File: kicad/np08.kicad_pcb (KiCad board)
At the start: 2 copper layers, 101.6 x 101.6 mm, 60 parts, among them P1 USB_B, P10 CONN_01X02, P11 CONN_01X02, P12 analog, P13 GND, P14 +5V, P15 CONN_01X08, P16 CONN_01X08, P2 CONN_01X04, P3 aliment., P4 sw_aliment, P5 sw_pic, P6 CONN_01X03, P7 CONN_01X03, P8 CONN_01X02, P9 CONN_01X02, SW1 SW_PUSH, U1 LM78L05ACZ, U2 LM7805CT, U3 L293D, U4 ULN2803, Y1 Crystal

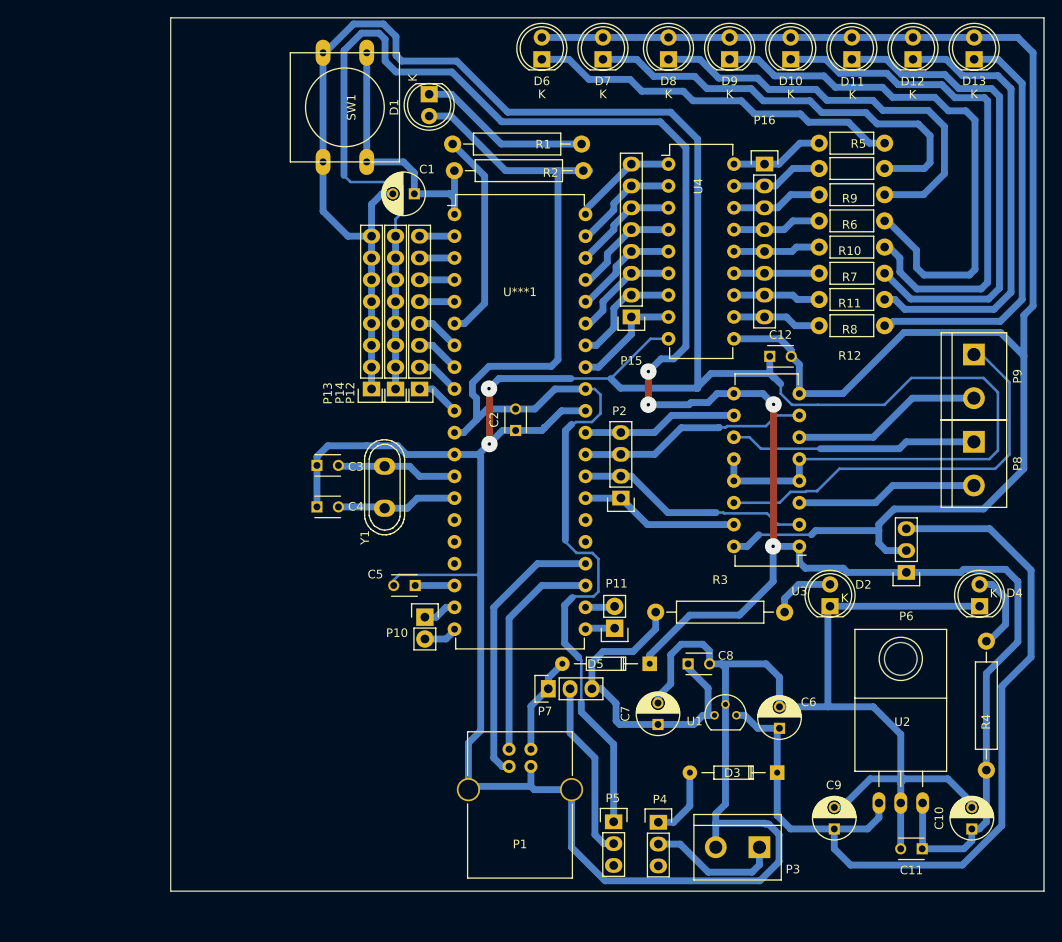
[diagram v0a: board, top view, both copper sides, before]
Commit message: cambios en la placa np08
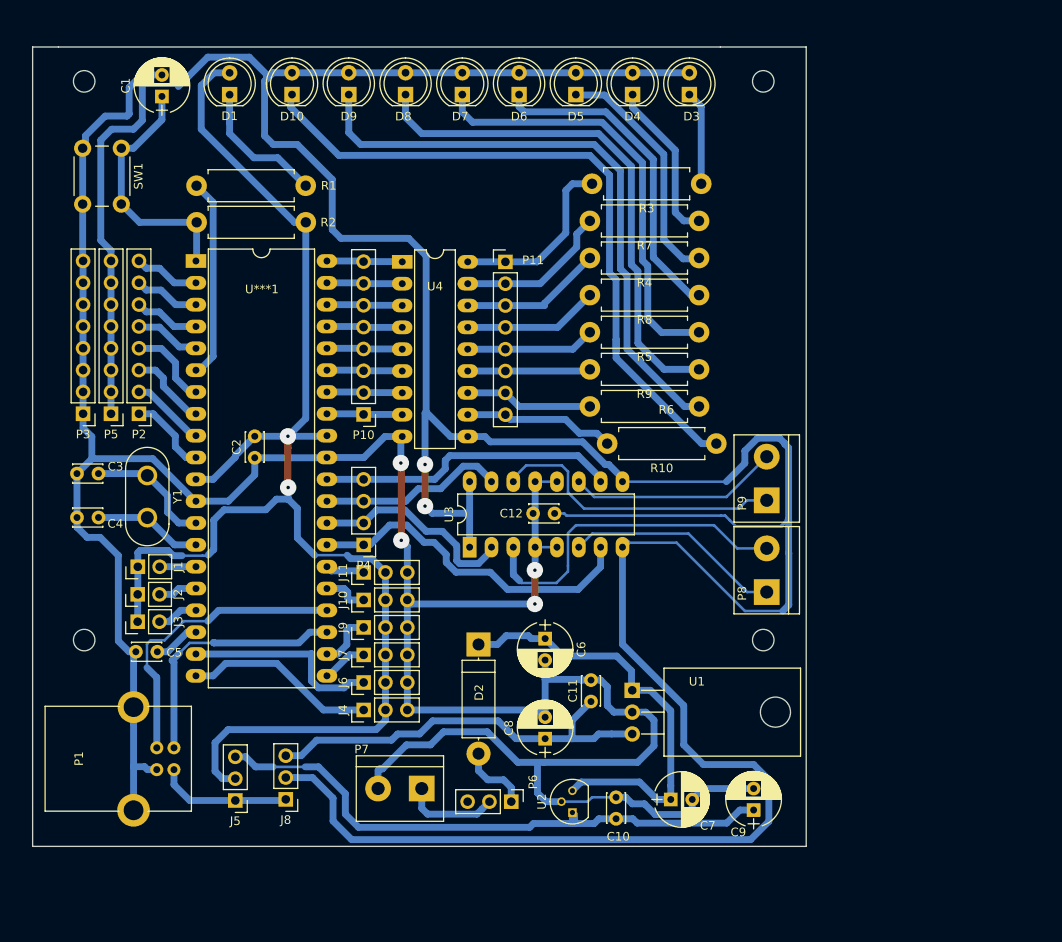
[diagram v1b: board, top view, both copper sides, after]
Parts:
- removed D11, D12, D13: LED, LEDs:LED-5MM
- removed P12: analog, Pin_Headers:Pin_Header_Straight_1x08
- removed P13: GND, Pin_Headers:Pin_Header_Straight_1x08
- removed P14: +5V, Pin_Headers:Pin_Header_Straight_1x08
- removed P15, P16: CONN_01X08, Pin_Headers:Pin_Header_Straight_1x08
- removed R11, R12: R, Resistors_ThroughHole:Resistor_Horizontal_RM7mm
- added ?: 2.5mm, Mounting_Holes:MountingHole_2.5mm, F.Cu at (89.0, 127.0)
- added ?: 2.5mm, Mounting_Holes:MountingHole_2.5mm, F.Cu at (168.0, 127.0)
- added ?: 2.5mm, Mounting_Holes:MountingHole_2.5mm, F.Cu at (168.0, 62.0)
- added ?: 2.5mm, Mounting_Holes:MountingHole_2.5mm, F.Cu at (89.0, 62.0)
- added J1: SENS_D3, Pin_Headers:Pin_Header_Straight_1x02_Pitch2.54mm, F.Cu at (95.2, 118.5)
- added J10: SRV2, Pin_Headers:Pin_Header_Straight_1x03_Pitch2.54mm, F.Cu at (121.5, 122.3)
- added J11: SRV1, Pin_Headers:Pin_Header_Straight_1x03_Pitch2.54mm, F.Cu at (121.5, 119.1)
- added J2: SENS_D2, Pin_Headers:Pin_Header_Straight_1x02_Pitch2.54mm, F.Cu at (95.2, 121.7)
- added J3: SENS_D1, Pin_Headers:Pin_Header_Straight_1x02_Pitch2.54mm, F.Cu at (95.2, 124.9)
- added J4: SRV6, Pin_Headers:Pin_Header_Straight_1x03_Pitch2.54mm, F.Cu at (121.5, 135.1)
- added J5: USB-78L05, Pin_Headers:Pin_Header_Straight_1x03_Pitch2.54mm, F.Cu at (106.6, 145.7)
- added J6: SRV5, Pin_Headers:Pin_Header_Straight_1x03_Pitch2.54mm, F.Cu at (121.5, 131.9)
- added J7: SRV4, Pin_Headers:Pin_Header_Straight_1x03_Pitch2.54mm, F.Cu at (121.5, 128.7)
- added J8: USB-LM7805, Pin_Headers:Pin_Header_Straight_1x03_Pitch2.54mm, F.Cu at (112.5, 145.5)
- added J9: SRV3, Pin_Headers:Pin_Header_Straight_1x03_Pitch2.54mm, F.Cu at (121.5, 125.5)
- C1, C6: footprint Capacitors_ThroughHole:C_Radial_D5_L6_P2.5 -> Capacitors_THT:CP_Radial_D6.3mm_P2.50mm
- C10: value 100 uF-electr -> 0.1uF; footprint Capacitors_ThroughHole:C_Radial_D5_L6_P2.5 -> Capacitors_THT:C_Disc_D3.4mm_W2.1mm_P2.50mm
- C11, C12, C2, C3, C4, C5: footprint Capacitors_ThroughHole:C_Disc_D3_P2.5 -> Capacitors_THT:C_Disc_D3.4mm_W2.1mm_P2.50mm
- C7: value 100 uF-electr -> 100uF-electr; footprint Capacitors_ThroughHole:C_Radial_D5_L6_P2.5 -> Capacitors_THT:CP_Radial_D6.3mm_P2.50mm
- C8: value 0.1uF -> 100 uF-electr; footprint Capacitors_ThroughHole:C_Disc_D3_P2.5 -> Capacitors_THT:CP_Radial_D6.3mm_P2.50mm
- C9: value 100uF-electr -> 100 uF-electr; footprint Capacitors_ThroughHole:C_Radial_D5_L6_P2.5 -> Capacitors_THT:CP_Radial_D6.3mm_P2.50mm
- D1: value LED -> RUN; footprint LEDs:LED-5MM -> LEDs:LED_D5.0mm
- D10: value LED -> LED_128; footprint LEDs:LED-5MM -> LEDs:LED_D5.0mm
- D2: value LED -> D; footprint LEDs:LED-5MM -> Diodes_THT:D_5W_P12.70mm_Horizontal
- D3: value D -> LED_1; footprint Diodes_ThroughHole:Diode_DO-35_SOD27_Horizontal_RM10 -> LEDs:LED_D5.0mm
- D4: value LED -> LED_2; footprint LEDs:LED-5MM -> LEDs:LED_D5.0mm
- D5: value D -> LED_4; footprint Diodes_ThroughHole:Diode_DO-35_SOD27_Horizontal_RM10 -> LEDs:LED_D5.0mm
- D6: value LED -> LED_8; footprint LEDs:LED-5MM -> LEDs:LED_D5.0mm
- D7: value LED -> LED_16; footprint LEDs:LED-5MM -> LEDs:LED_D5.0mm
- D8: value LED -> LED_32; footprint LEDs:LED-5MM -> LEDs:LED_D5.0mm
- D9: value LED -> LED_64; footprint LEDs:LED-5MM -> LEDs:LED_D5.0mm
- P1: footprint Connect:USB_B -> Connectors:USB_B
- P10, P11: value CONN_01X02 -> PORTB; footprint Pin_Headers:Pin_Header_Straight_1x02 -> Pin_Headers:Pin_Header_Straight_1x08_Pitch2.54mm
- P2: value CONN_01X04 -> analog; footprint Pin_Headers:Pin_Header_Straight_1x04 -> Pin_Headers:Pin_Header_Straight_1x08_Pitch2.54mm
- P3: value aliment. -> GND; footprint Connect:bornier2 -> Pin_Headers:Pin_Header_Straight_1x08_Pitch2.54mm
- P4: value sw_aliment -> PORTD=4-7; footprint Pin_Headers:Pin_Header_Straight_1x03 -> Pin_Headers:Pin_Header_Straight_1x04_Pitch2.54mm
- P5: value sw_pic -> +5V; footprint Pin_Headers:Pin_Header_Straight_1x03 -> Pin_Headers:Pin_Header_Straight_1x08_Pitch2.54mm
- P6: value CONN_01X03 -> sw_aliment; footprint Pin_Headers:Pin_Header_Straight_1x03 -> Pin_Headers:Pin_Header_Straight_1x03_Pitch2.54mm
- P7: value CONN_01X03 -> - +; footprint Pin_Headers:Pin_Header_Straight_1x03 -> Connectors:bornier2
- P8: value CONN_01X02 -> MOTOR_2; footprint Connect:bornier2 -> Connectors:bornier2
- P9: value CONN_01X02 -> MOTOR_1; footprint Connect:bornier2 -> Connectors:bornier2
- R1, R2: footprint Resistors_ThroughHole:Resistor_Horizontal_RM15mm -> Resistors_THT:R_Axial_DIN0411_L9.9mm_D3.6mm_P12.70mm_Horizontal
- R10, R5, R6, R7, R8, R9: footprint Resistors_ThroughHole:Resistor_Horizontal_RM7mm -> Resistors_THT:R_Axial_DIN0411_L9.9mm_D3.6mm_P12.70mm_Horizontal
- R3, R4: value 470 -> R; footprint Resistors_ThroughHole:Resistor_Horizontal_RM15mm -> Resistors_THT:R_Axial_DIN0411_L9.9mm_D3.6mm_P12.70mm_Horizontal
- SW1: value SW_PUSH -> RESET; footprint Buttons_Switches_ThroughHole:SW_PUSH-12mm -> Buttons_Switches_THT:SW_PUSH_6mm_h5mm
- U***1: footprint Housings_DIP:DIP-40_W15.24mm -> Housings_DIP:DIP-40_W15.24mm_LongPads
- U1: value LM78L05ACZ -> LM7805CT; footprint TO_SOT_Packages_THT:TO-92_Molded_Narrow -> TO_SOT_Packages_THT:TO-220_Horizontal
- U2: value LM7805CT -> LM78L05ACZ; footprint TO_SOT_Packages_THT:TO-220_Neutral123_Horizontal -> TO_SOT_Packages_THT:TO-92_Molded_Narrow
- U3: footprint Housings_DIP:DIP-16_W7.62mm -> Housings_DIP:DIP-16_W7.62mm_LongPads
- U4: footprint Housings_DIP:DIP-18_W7.62mm -> Housings_DIP:DIP-18_W7.62mm_LongPads
- Y1: footprint Crystals:Crystal_HC50-U_Vertical -> Crystals:Crystal_HC50_Vertical
- moved P3 91.3 mm to (88.9, 100.7)
- moved D3 79.5 mm to (159.4, 63.5), turned to 90 degrees
- moved P5 75.3 mm to (92.1, 100.7), turned to 180 degrees
- moved D4 71.9 mm to (152.8, 63.5)
- moved R4 68.3 mm to (160.5, 82.5), turned to 180 degrees
- moved D5 66.8 mm to (146.2, 63.5), turned to 90 degrees
- moved D10 58.2 mm to (113.2, 63.5)
- moved P2 56.9 mm to (95.4, 100.7)
- moved P6 53.1 mm to (138.7, 145.8), turned to 270 degrees
- moved R3 50.1 mm to (160.8, 73.9), turned to 180 degrees
- moved P4 47.1 mm to (121.5, 115.9), turned to 180 degrees
- moved D9 44.5 mm to (119.8, 63.5)
- moved P11 44.5 mm to (138.0, 83.0), turned to 0 degrees
- moved C11 42.2 mm to (148.0, 134.2), turned to 90 degrees
- moved P1 41.6 mm to (99.4, 142.1), turned to 180 degrees
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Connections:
- C10 pad 1: /alimentacion/5v_lm7805 -> 5v_reg_pic
- C11 pad 1: /alimentacion/5v_lm7805 -> 5v_reg
- C12 pad 2: /UNL2803/+5/12V -> 5v
- C7 pad 1: /alimentacion/5v_78l05 -> 12V
- C8 pad 1: /alimentacion/5v_78l05 -> 5v_reg
- C9 pad 1: 12V -> 5v_reg_pic
- D10 pad 2: /UNL2803/+5/12V -> 5v
- D2 pad 1: GND -> 12V
- D3 pad 1: 12V -> Net-(D3-Pad1)
- D3 pad 2: Net-(D3-Pad2) -> 5v
- D4 pad 1: GND -> Net-(D4-Pad1)
- D4 pad 2: Net-(D4-Pad2) -> 5v
- D5 pad 1: /alimentacion/5v_lm7805 -> Net-(D5-Pad1)
- D5 pad 2: VCC -> 5v
- D6 pad 2: /UNL2803/+5/12V -> 5v
- D7 pad 2: /UNL2803/+5/12V -> 5v
- D8 pad 2: /UNL2803/+5/12V -> 5v
- D9 pad 2: /UNL2803/+5/12V -> 5v
- P1 pad 1: VCC -> 5v_reg_usb
- P10 pad 1: RD0 -> IN7
- P10 pad 2: RD1 -> IN6
- P11 pad 1: RD2 -> OOUT_0
- P11 pad 2: RD3 -> OOUT_1
- P2 pad 1: RD4 -> Net-(P2-Pad1)
- P2 pad 2: RD5 -> Net-(P2-Pad2)
- P2 pad 3: RD6 -> Net-(P2-Pad3)
- P2 pad 4: RD7 -> Net-(P2-Pad4)
- P3 pad 1: Net-(P3-Pad1) -> GND
- P4 pad 1: Net-(D3-Pad2) -> RD4
- P4 pad 2: Net-(P3-Pad1) -> RD5
- P4 pad 3: (no net) -> RD6
- P5 pad 1: VDD -> 5v
- P5 pad 2: vcc_con -> 5v
- P5 pad 3: (no net) -> 5v
- P6 pad 1: /alimentacion/5v_lm7805 -> Net-(D2-Pad2)
- P6 pad 2: /UNL2803/+5/12V -> Net-(P6-Pad2)
- P6 pad 3: 12V -> (no net)
- P7 pad 1: VCC -> Net-(P6-Pad2)
- P7 pad 2: vcc_con -> GND
- R10 pad 1: Net-(D9-Pad1) -> Net-(D10-Pad1)
- R10 pad 2: OOUT_3 -> OOUT_7
- R3 pad 1: /alimentacion/5v_78l05 -> Net-(D3-Pad1)
- R3 pad 2: Net-(D2-Pad2) -> OOUT_0
- R4 pad 1: /alimentacion/5v_lm7805 -> Net-(D5-Pad1)
- R4 pad 2: Net-(D4-Pad2) -> OOUT_2
- R5 pad 1: Net-(D6-Pad1) -> Net-(D7-Pad1)
- R5 pad 2: OOUT_0 -> OOUT_4
- R6 pad 1: Net-(D8-Pad1) -> Net-(D9-Pad1)
- R6 pad 2: OOUT_2 -> OOUT_6
- R7 pad 1: Net-(D10-Pad1) -> Net-(D4-Pad1)
- R7 pad 2: OOUT_4 -> OOUT_1
- R8 pad 1: Net-(D12-Pad1) -> Net-(D6-Pad1)
- R8 pad 2: OOUT_6 -> OOUT_3
- R9 pad 1: Net-(D7-Pad1) -> Net-(D8-Pad1)
- R9 pad 2: OOUT_1 -> OOUT_5
- U***1 pad 10: Net-(P12-Pad1) -> Net-(P2-Pad1)
- U***1 pad 15: (no net) -> RC0
- U***1 pad 16: (no net) -> RC1
- U***1 pad 17: (no net) -> RC2
- U***1 pad 2: Net-(P12-Pad8) -> Net-(P2-Pad8)
- U***1 pad 25: (no net) -> RC6
- U***1 pad 26: (no net) -> RC7
- U***1 pad 3: Net-(P12-Pad7) -> Net-(P2-Pad7)
- U***1 pad 4: Net-(P12-Pad6) -> Net-(P2-Pad6)
- U***1 pad 5: Net-(P12-Pad5) -> Net-(P2-Pad5)
- U***1 pad 7: Net-(P12-Pad4) -> Net-(P2-Pad4)
- U***1 pad 8: Net-(P12-Pad3) -> Net-(P2-Pad3)
- U***1 pad 9: Net-(P12-Pad2) -> Net-(P2-Pad2)
- U1 pad 1: /alimentacion/5v_78l05 -> 12V
- U1 pad 3: 12V -> 5v_reg
- U2 pad 1: 12V -> 5v_reg_pic
- U2 pad 3: /alimentacion/5v_lm7805 -> 12V
- U3 pad 1: /alimentacion/5v_lm7805 -> 5v
- U3 pad 11: Net-(P8-Pad1) -> Net-(P9-Pad2)
- U3 pad 15: RD4 -> RD6
- U3 pad 16: /UNL2803/+5/12V -> 5v
- U3 pad 6: Net-(P9-Pad2) -> Net-(P8-Pad1)
- U3 pad 7: RD6 -> RD4
- U3 pad 8: /UNL2803/+5/12V -> 5v
- U3 pad 9: /alimentacion/5v_lm7805 -> 5v
- U4 pad 10: /UNL2803/+5/12V -> 5v
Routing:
- net 5v: track 0.00 -> 422.9 mm, vias 0 -> 2
- net /alimentacion/5v_lm7805: track 257.1 -> 0.00 mm, vias 4 -> 0
- net GND: track 543.2 -> 323.0 mm, vias 2 -> 4
- net /UNL2803/+5/12V: track 192.5 -> 0.00 mm
- net 5v_reg_pic: track 0.00 -> 68.7 mm
- net Net-(D11-Pad1): track 56.4 -> 0.00 mm
- net Net-(D12-Pad1): track 52.5 -> 0.00 mm
- net 12V: track 102.8 -> 50.6 mm
- net Net-(D13-Pad1): track 49.9 -> 0.00 mm
- net 5v_reg: track 0.00 -> 48.7 mm
- net /alimentacion/5v_78l05: track 38.6 -> 0.00 mm
- net VDD: track 138.9 -> 173.9 mm, vias 0 -> 2
- net Net-(D5-Pad1): track 0.00 -> 28.2 mm
- net RD4: track 18.5 -> 39.8 mm
- net vcc_con: track 20.8 -> 0.00 mm
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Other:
- board size 101.6 x 101.6 mm -> 90 x 93 mm
- net class fina: trace_width 0.3 -> 0.5

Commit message: arreglando la fuente de alimentación, los servos estaban conectados al 78l05
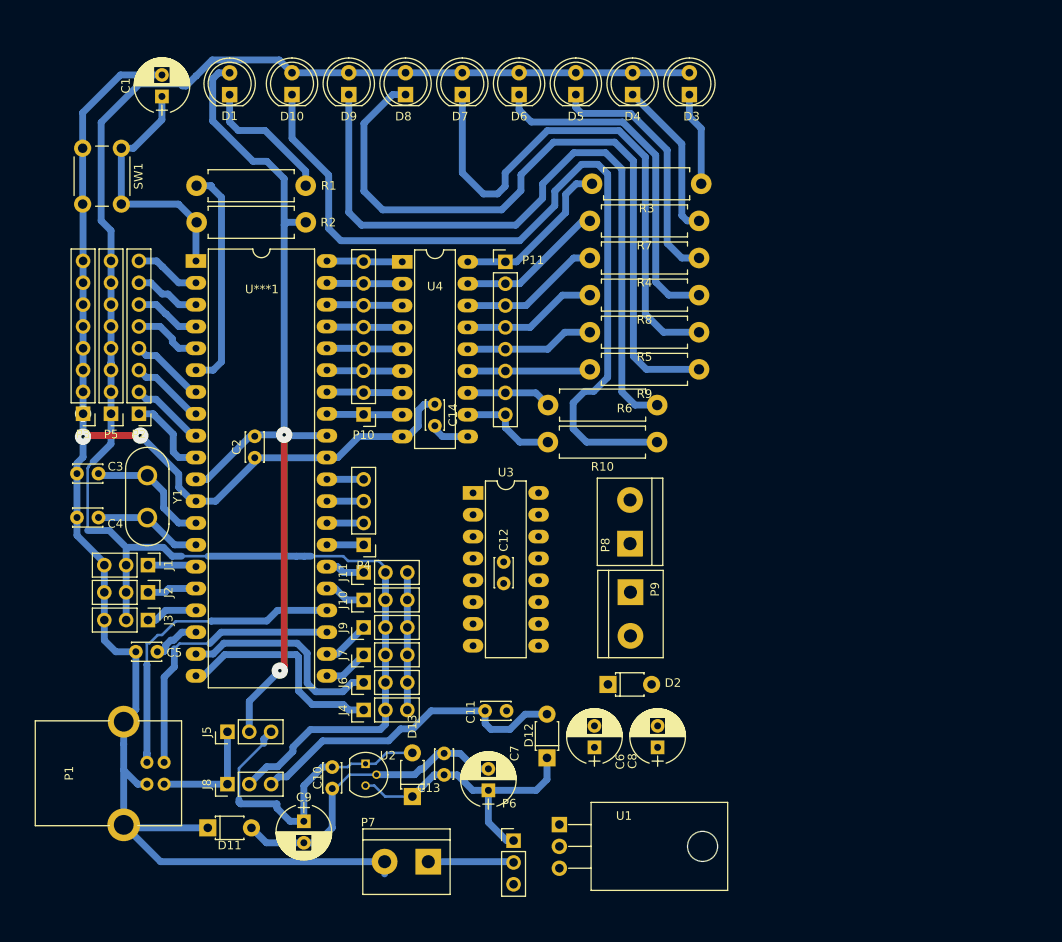
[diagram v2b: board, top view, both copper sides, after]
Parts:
- removed ? (x4): 2.5mm, Mounting_Holes:MountingHole_2.5mm
- added C13: 0.1uF, Capacitors_THT:C_Disc_D3.4mm_W2.1mm_P2.50mm, F.Cu at (130.9, 142.7)
- added C14: 0.1uF, Capacitors_THT:C_Disc_D3.4mm_W2.1mm_P2.50mm, F.Cu at (129.8, 99.6)
- added D11: D, Diodes_THT:D_T-1_P5.08mm_Horizontal, F.Cu at (103.4, 148.8)
- added D12: D, Diodes_THT:D_T-1_P5.08mm_Horizontal, F.Cu at (142.8, 140.7)
- added D13: D, Diodes_THT:D_T-1_P5.08mm_Horizontal, F.Cu at (127.2, 145.2)
- C6, C7: value 100uF-electr -> 220uF-electr
- C8, C9: value 100 uF-electr -> 220uF-electr
- D2: footprint Diodes_THT:D_5W_P12.70mm_Horizontal -> Diodes_THT:D_T-1_P5.08mm_Horizontal
- J1: value SENS_D3 -> SENS_D1; footprint Pin_Headers:Pin_Header_Straight_1x02_Pitch2.54mm -> Pin_Headers:Pin_Header_Straight_1x03_Pitch2.54mm
- J2: footprint Pin_Headers:Pin_Header_Straight_1x02_Pitch2.54mm -> Pin_Headers:Pin_Header_Straight_1x03_Pitch2.54mm
- J3: value SENS_D1 -> SENS_D3; footprint Pin_Headers:Pin_Header_Straight_1x02_Pitch2.54mm -> Pin_Headers:Pin_Header_Straight_1x03_Pitch2.54mm
- P7: value - + -> aliment.
- U1: value LM7805CT -> LM7805
- U2: value LM78L05ACZ -> LM78L05
- moved C9 52.3 mm to (114.6, 148.1), turned to 270 degrees
- moved C10 33.6 mm to (117.9, 141.8), turned to 270 degrees
- moved U2 24.7 mm to (121.7, 141.4), turned to 270 degrees
- moved C7 21.2 mm to (136.0, 144.5), turned to 90 degrees
- moved P9 19.1 mm to (152.6, 121.4), turned to 270 degrees
- moved U1 17.8 mm to (144.3, 148.5)
- moved P8 16.9 mm to (152.5, 115.8)
- moved D2 15.8 mm to (149.9, 132.2), turned to 0 degrees
- moved C6 13.9 mm to (148.4, 139.5), turned to 90 degrees
- moved C8 13.1 mm to (155.7, 139.5)
- moved C11 12.4 mm to (135.6, 135.2), turned to 0 degrees
- moved P7 8.54 mm to (129.0, 152.8)
- moved J5 8.04 mm to (105.7, 137.7), turned to 90 degrees
- moved J8 7.01 mm to (105.7, 143.8), turned to 90 degrees
- moved R10 6.90 mm to (155.6, 104.0)
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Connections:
- C10 pad 2: GND -> Net-(C10-Pad2)
- C11 pad 2: GND -> Net-(C11-Pad2)
- C6 pad 2: GND -> Net-(C11-Pad2)
- C7 pad 2: GND -> Net-(C10-Pad2)
- C8 pad 2: GND -> Net-(C11-Pad2)
- C9 pad 2: GND -> Net-(C10-Pad2)
- D2 pad 1: 12V -> GND
- D2 pad 2: Net-(D2-Pad2) -> Net-(C11-Pad2)
- J1 pad 1: VDD -> RC0
- J1 pad 2: RC0 -> 5v
- J10 pad 2: VDD -> 5v
- J11 pad 2: VDD -> 5v
- J2 pad 1: VDD -> RC1
- J2 pad 2: RC1 -> 5v
- J3 pad 1: VDD -> RC2
- J3 pad 2: RC2 -> 5v
- J4 pad 2: VDD -> 5v
- J6 pad 2: VDD -> 5v
- J7 pad 2: VDD -> 5v
- J9 pad 2: VDD -> 5v
- P6 pad 1: Net-(D2-Pad2) -> 12V
- U1 pad 2: GND -> Net-(C11-Pad2)
- U2 pad 2: GND -> Net-(C10-Pad2)
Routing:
- net 5v: track 422.9 -> 215.6 mm, vias 2 -> 0
- net GND: track 323.0 -> 212.9 mm, vias 4 -> 3
- net VDD: track 173.9 -> 104.4 mm
- net Net-(P8-Pad2): track 39.6 -> 0.00 mm
- net Net-(C10-Pad2): track 0.00 -> 36.0 mm
- net RD4: track 39.8 -> 5.00 mm
- net Net-(P9-Pad1): track 34.4 -> 0.00 mm
- net 5v_reg_pic: track 68.7 -> 36.9 mm
- net RD7: track 35.0 -> 4.27 mm
- net Net-(P8-Pad1): track 25.3 -> 0.00 mm
- net Net-(P9-Pad2): track 24.5 -> 0.00 mm
- net Net-(D8-Pad1): track 60.5 -> 82.6 mm
- net RD5: track 24.4 -> 4.27 mm
- net RD6: track 21.7 -> 4.27 mm
- net Net-(D10-Pad1): track 80.7 -> 97.9 mm
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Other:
- board outline removed

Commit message: cambios para el desarrollo de la placa np08, ahora usa 6 pines para servos y 3 pines para dig
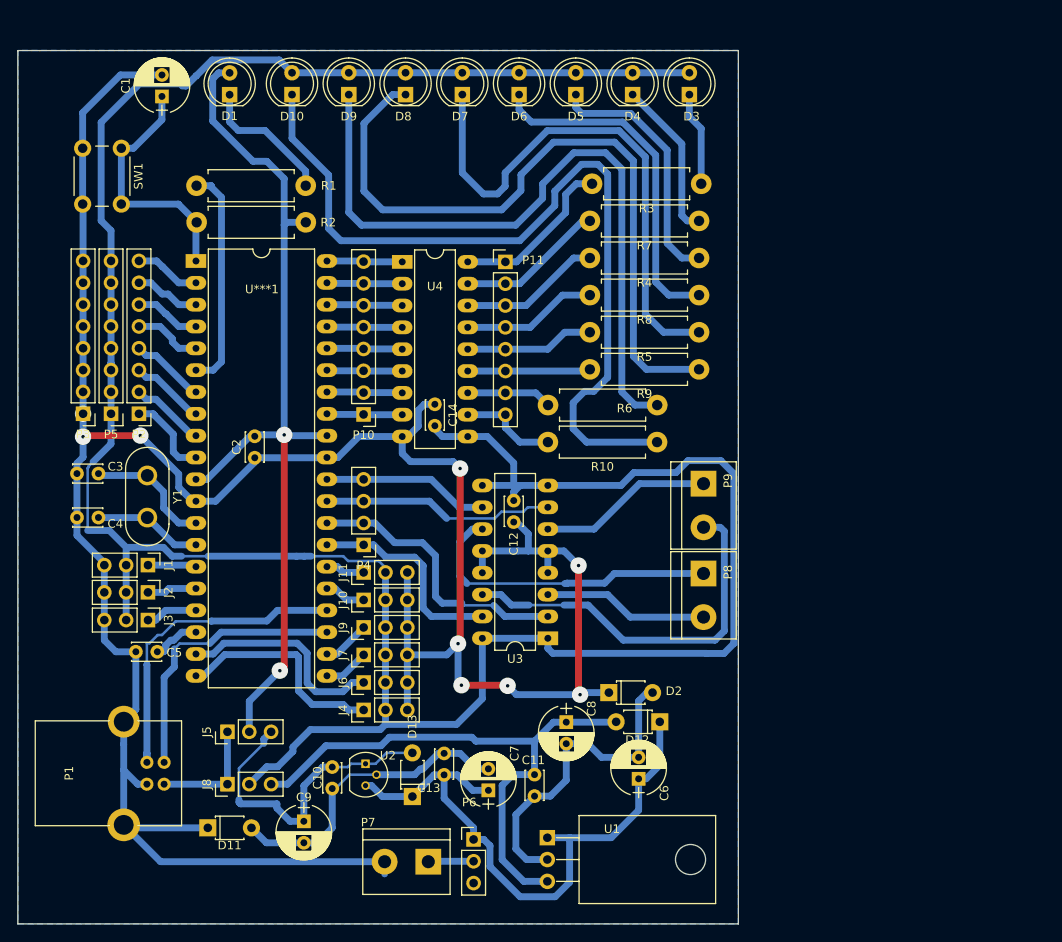
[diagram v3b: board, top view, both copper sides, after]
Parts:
- moved U3 19.0 mm to (142.9, 126.8), turned to 180 degrees
- moved P9 15.2 mm to (161.1, 108.8)
- moved D12 13.8 mm to (156.0, 136.5), turned to 180 degrees
- moved C8 11.0 mm to (145.1, 136.6), turned to 270 degrees
- moved C11 9.39 mm to (141.4, 142.7), turned to 270 degrees
- moved P8 9.23 mm to (161.1, 119.2), turned to 270 degrees
- moved C6 6.31 mm to (153.5, 143.1)
- moved C12 4.79 mm to (139.0, 113.3), turned to 90 degrees
- moved P6 4.65 mm to (134.3, 150.2)
- moved U1 2.07 mm to (142.9, 150.0)
- moved D2 0.96 mm to (150.0, 133.1)
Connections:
- U3 pad 11: Net-(P9-Pad2) -> Net-(P8-Pad1)
- U3 pad 14: Net-(P9-Pad1) -> Net-(P9-Pad2)
- U3 pad 15: RD6 -> RD4
- U3 pad 6: Net-(P8-Pad1) -> Net-(P9-Pad1)
- U3 pad 7: RD4 -> RD6
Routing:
- net 5v: track 215.6 -> 328.8 mm
- net GND: track 212.9 -> 308.3 mm, vias 3 -> 9
- net Net-(P9-Pad2): track 0.00 -> 48.7 mm
- net Net-(P8-Pad1): track 0.00 -> 43.6 mm
- net Net-(C11-Pad2): track 0.00 -> 37.6 mm
- net 12V: track 34.0 -> 70.5 mm
- net RD5: track 4.27 -> 34.8 mm
- net 5v_reg: track 38.1 -> 67.3 mm
- net RD6: track 4.27 -> 27.1 mm
- net Net-(P9-Pad1): track 0.00 -> 20.3 mm
- net RD4: track 5.00 -> 25.2 mm
- net Net-(P8-Pad2): track 0.00 -> 19.2 mm
- net RD7: track 4.27 -> 19.4 mm
- net Net-(P6-Pad2): track 9.96 -> 5.29 mm
- added copper zone on B.Cu, net GND
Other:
- board outline added: 83.8 x 101.6 mm
